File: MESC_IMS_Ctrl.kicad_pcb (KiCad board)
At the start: 2 copper layers, 100 x 75 mm, 194 parts, among them J1 Conn_01x08_Female, J10 Conn_01x04_Male, J2 Conn_01x08_Female, J3 Conn_01x08_Female, J4 Conn_01x06_Male, J5 Conn_ARM_JTAG_SWD_10, J6 USB_C_Receptacle_USB2.0, J7 Conn_01x03_Male, J8 Conn_01x04_Male, J9 Conn_01x08_Male, U1 STM32F303CBTx, U10 TPS61041DBV, U2 LM5017MR, U3 TPS76333, U4 INA240A1PW, U5 UCC21520DW, U6 INA240A1PW, U7 UCC21520DW, U8 INA240A1PW, U9 UCC21520DW, Y1 ASE-8.000MHZ-LC-T

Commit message: More routing
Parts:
- moved TP4 9.06 mm to (132.2, 85.5)
- moved R40 3.05 mm to (112.5, 114.0), turned to 270 degrees
- moved R27 1.46 mm to (128.2, 134.0), turned to 0 degrees
- moved R41 1.34 mm to (112.5, 116.0), turned to 270 degrees
- moved C15 1.27 mm to (128.2, 135.2)
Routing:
- net /ISU_MCU: track 14.7 -> 60.9 mm, vias 0 -> 2
- net /U_I_SEN: track 13.1 -> 57.4 mm, vias 0 -> 2
- net /W_V_SEN: track 96.0 -> 122.5 mm, vias 1 -> 2
- net /V_SEN: track 101.3 -> 127.6 mm, vias 0 -> 2
- net VDD: track 97.3 -> 122.0 mm, vias 8 -> 10
- net /V_V_SEN: track 74.2 -> 98.4 mm, vias 2 -> 4
- net /PWM_IN: track 48.1 -> 51.0 mm
- net /U_IN_LO: track 40.9 -> 42.0 mm, vias 1 -> 2
- net /U_V_SEN: track 92.0 -> 93.1 mm
- net /U_IN_HI: track 41.7 -> 42.8 mm, vias 1 -> 2
- net +3V3: track 334.0 -> 333.1 mm, vias 30 -> 33
- net /ISV_MCU: track 47.4 -> 46.7 mm
- net /ANA_IN: track 43.7 -> 43.2 mm
- net /TMP_INT: track 67.9 -> 68.3 mm, vias 2 -> 4
- net GND: vias 90 -> 91

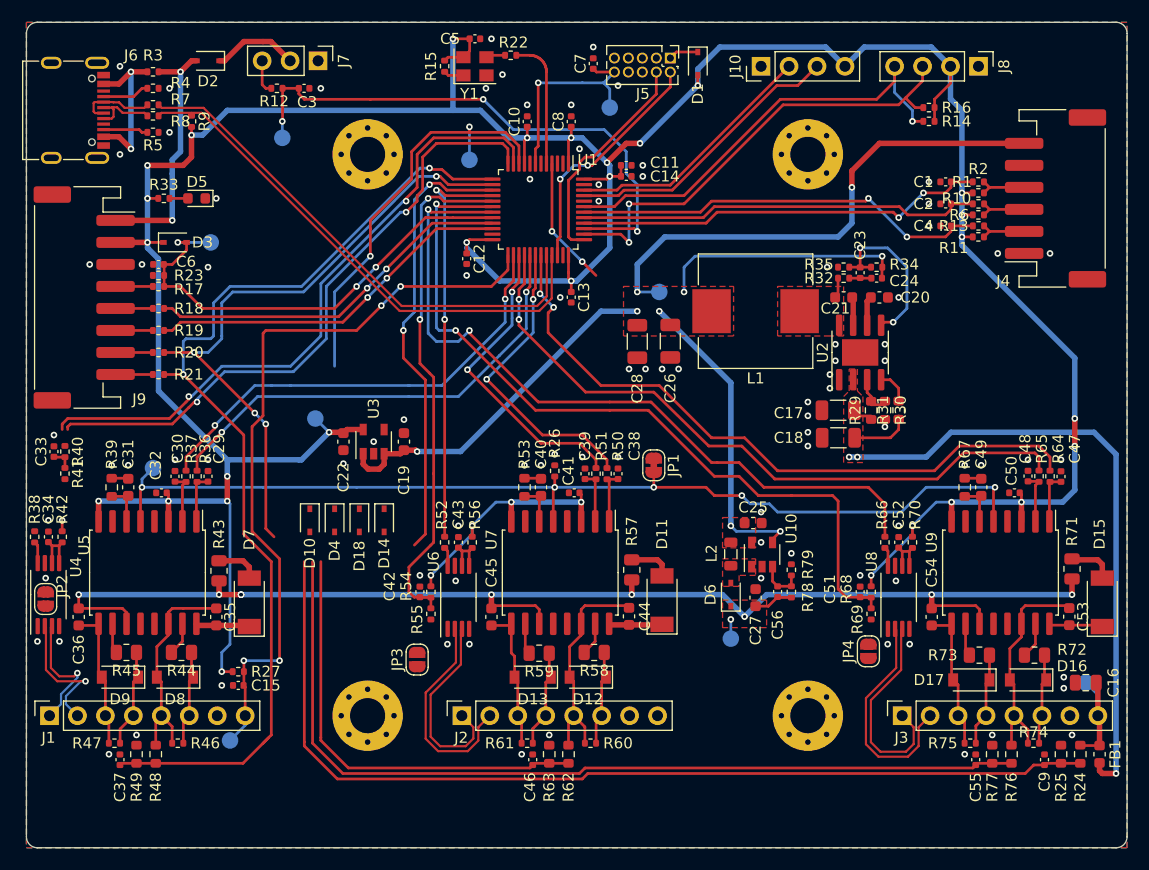
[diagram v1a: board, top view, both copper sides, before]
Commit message: Routing nearly complete
some diodes made smaller
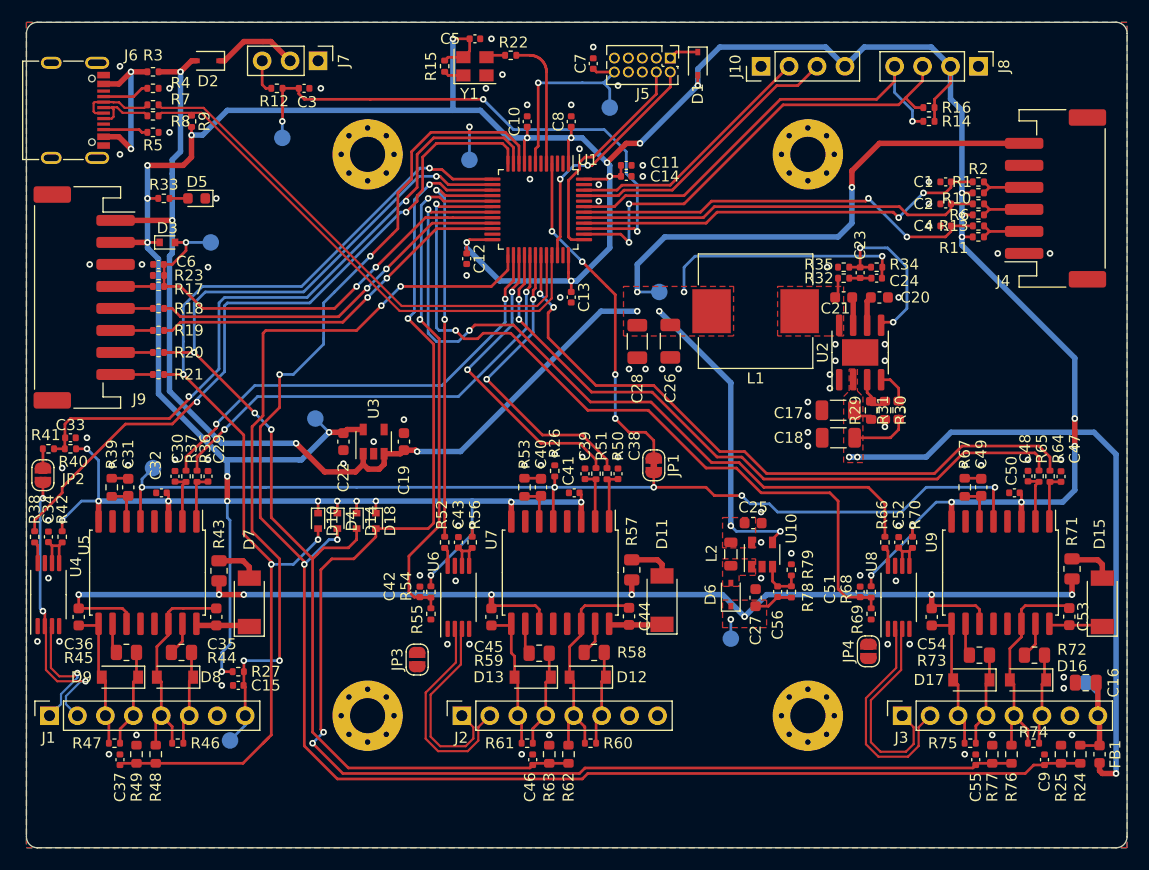
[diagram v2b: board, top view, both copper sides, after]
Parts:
- D10, D14, D18, D3, D4: value NSR1020MW2T1G -> BAT41KFILM; footprint Diode_SMD:D_SOD-323 -> Diode_SMD:D_SOD-523
- moved JP2 11.3 mm to (110.5, 116.2)
- moved R41 2.70 mm to (111.0, 113.8), turned to 180 degrees
- moved D14 2.50 mm to (139.0, 120.3)
- moved C33 1.95 mm to (113.0, 112.8), turned to 0 degrees
- moved D18 1.50 mm to (140.8, 120.3)
- moved D10 0.75 mm to (135.5, 120.3)
- moved D3 0.70 mm to (121.8, 95.0)
- moved R40 0.56 mm to (113.0, 113.8), turned to 180 degrees
- moved D4 0.25 mm to (137.2, 120.3)
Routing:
- net +3V3: track 333.1 -> 371.1 mm, vias 33 -> 38
- net +5V: track 153.5 -> 190.1 mm, vias 11 -> 12
- net /V_SEN: track 127.6 -> 155.4 mm, vias 2 -> 5
- net /GATE_DIS: track 11.8 -> 31.5 mm, vias 2 -> 4
- net /Phase_U/CURR_SEN+: track 12.6 -> 25.9 mm, vias 1 -> 3
- net /V_V_SEN: track 98.4 -> 108.9 mm
- net /W_V_SEN: track 122.5 -> 132.3 mm, vias 2 -> 4
- net /U_I_SEN: track 57.4 -> 65.7 mm
- net /U_V_SEN: track 93.1 -> 99.5 mm, vias 2 -> 4
- net Net-(JP2-Pad2): track 0.00 -> 1.75 mm
- net /W_IN_HI: track 61.2 -> 62.6 mm
- net /ISU_MCU: track 60.9 -> 62.2 mm
- net /ANA_IN: track 43.2 -> 42.6 mm
- net VDD: vias 10 -> 9
- net GND: vias 91 -> 92

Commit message: Adding via stitching and teardrops
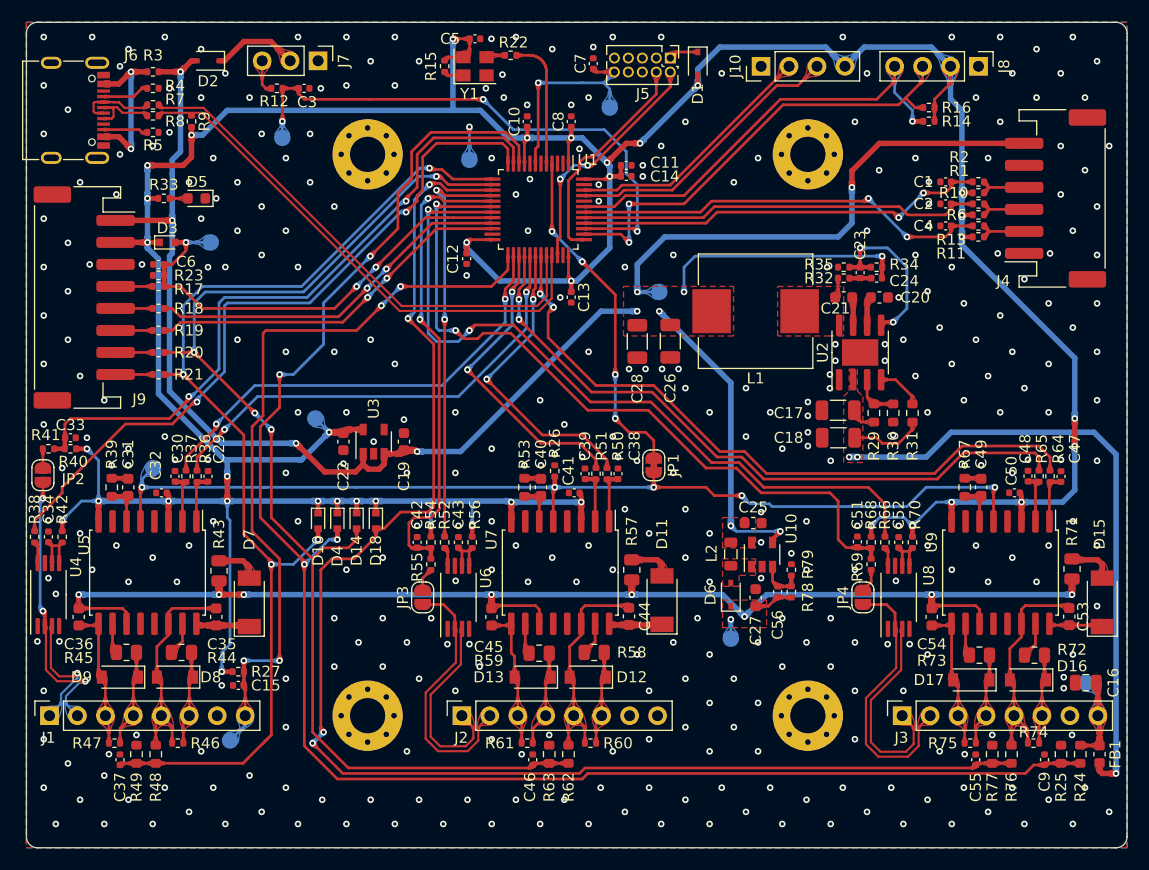
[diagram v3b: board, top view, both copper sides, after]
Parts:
- moved JP3 5.67 mm to (145.0, 127.2)
- moved JP4 4.93 mm to (185.0, 127.2)
- moved C51 4.56 mm to (184.5, 122.2)
- moved C42 4.51 mm to (144.5, 122.2)
- moved R54 4.50 mm to (145.8, 122.2)
- moved R55 4.50 mm to (145.8, 124.2)
- moved R68 4.50 mm to (185.8, 122.2)
- moved R69 4.50 mm to (185.8, 124.2)
- moved R31 1.28 mm to (189.5, 110.5)
- moved R30 0.79 mm to (187.8, 110.5)
- moved R29 0.35 mm to (186.0, 110.5)
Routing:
- net +3V3: track 371.1 -> 365.7 mm
- net /Phase_W/CURR_SEN+: track 20.5 -> 25.2 mm
- net /Phase_V/CURR_SEN+: track 19.5 -> 24.0 mm
- net /ISW_MCU: track 72.2 -> 67.7 mm
- net /ISV_MCU: track 47.2 -> 43.7 mm
- net Net-(JP4-Pad2): track 0.00 -> 2.15 mm
- net Net-(JP3-Pad2): track 0.00 -> 2.15 mm
- net /PSUs/VCC: track 64.6 -> 66.5 mm
- net /W_V_SEN: track 132.3 -> 131.4 mm
- net Net-(R31-Pad2): track 3.40 -> 4.15 mm
- net Net-(R29-Pad2): track 3.68 -> 4.20 mm
- net GND: vias 92 -> 369

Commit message: Updated part numbers
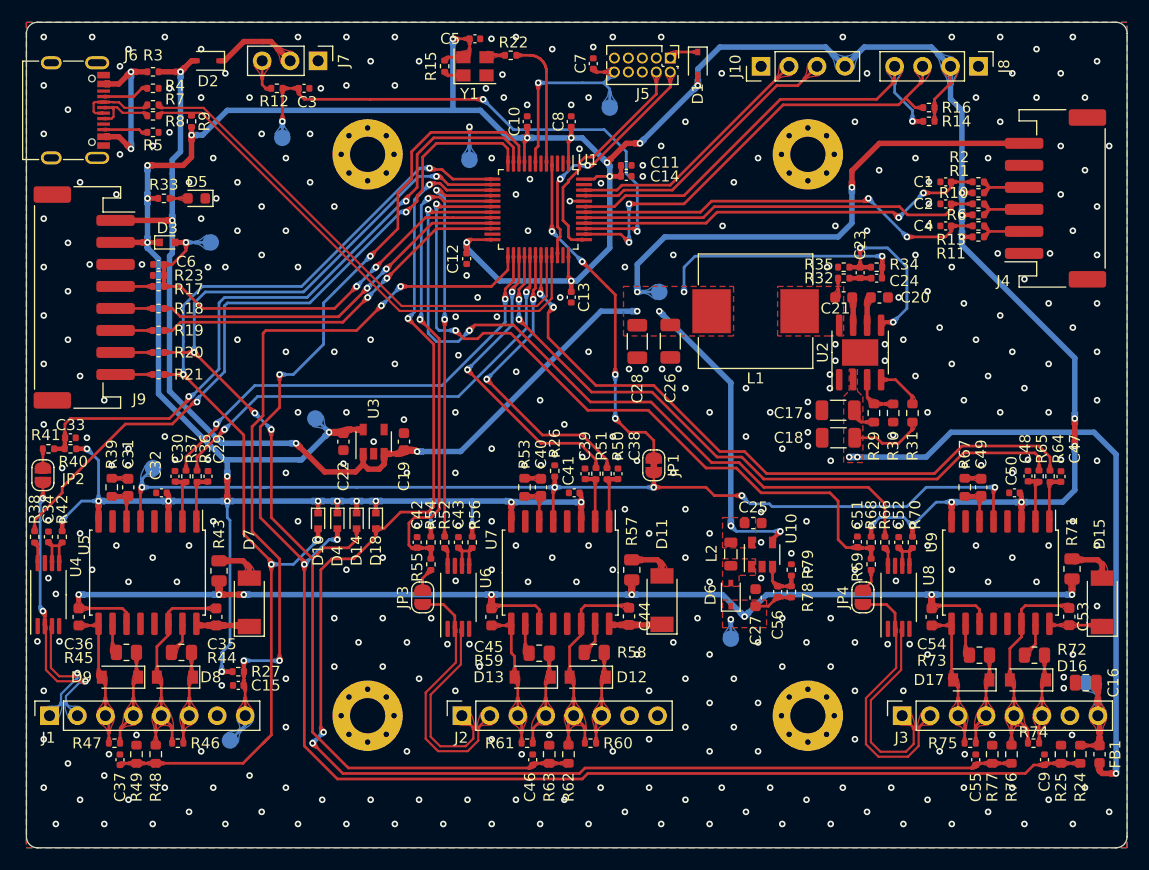
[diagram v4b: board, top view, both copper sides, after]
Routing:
- net GND: track 4.56 -> 5.85 mm, vias 369 -> 376
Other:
- rule via_min_size: 0.3 -> 0.2

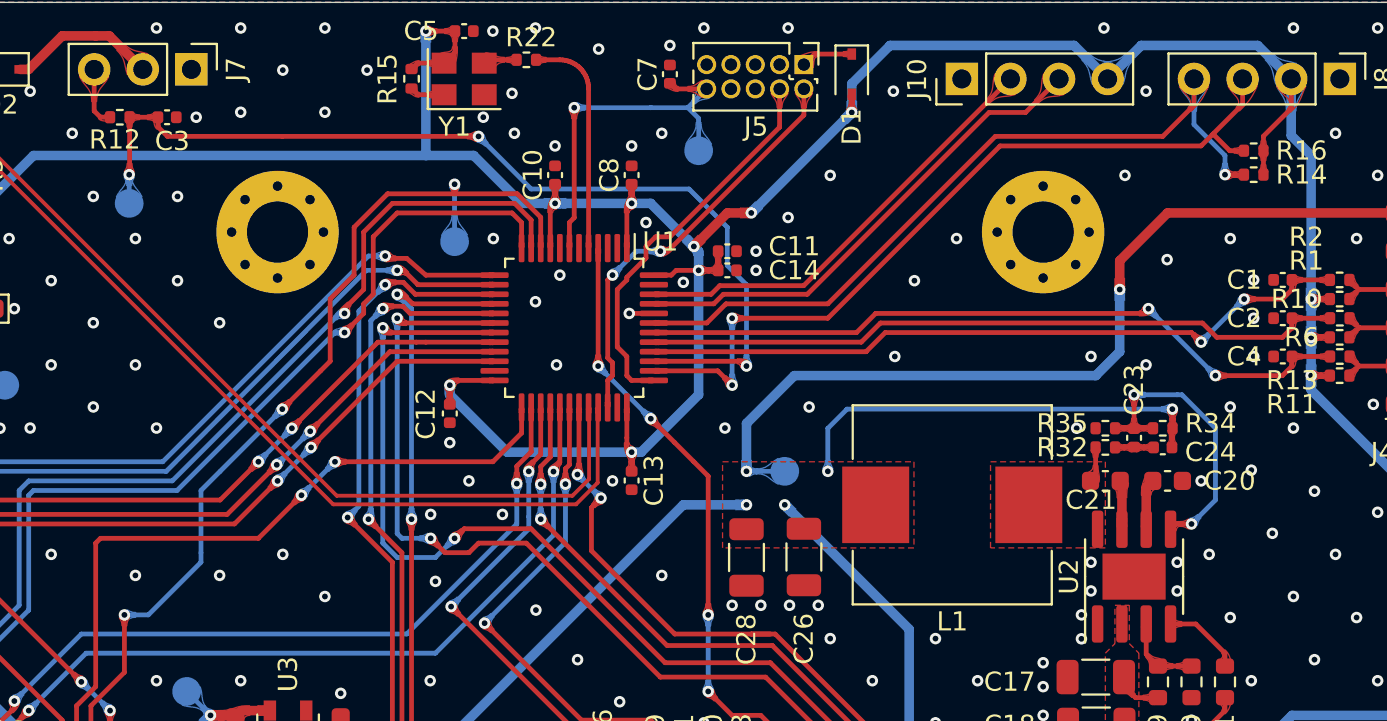
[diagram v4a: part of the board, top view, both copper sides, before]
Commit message: Adding 0V TP and labels
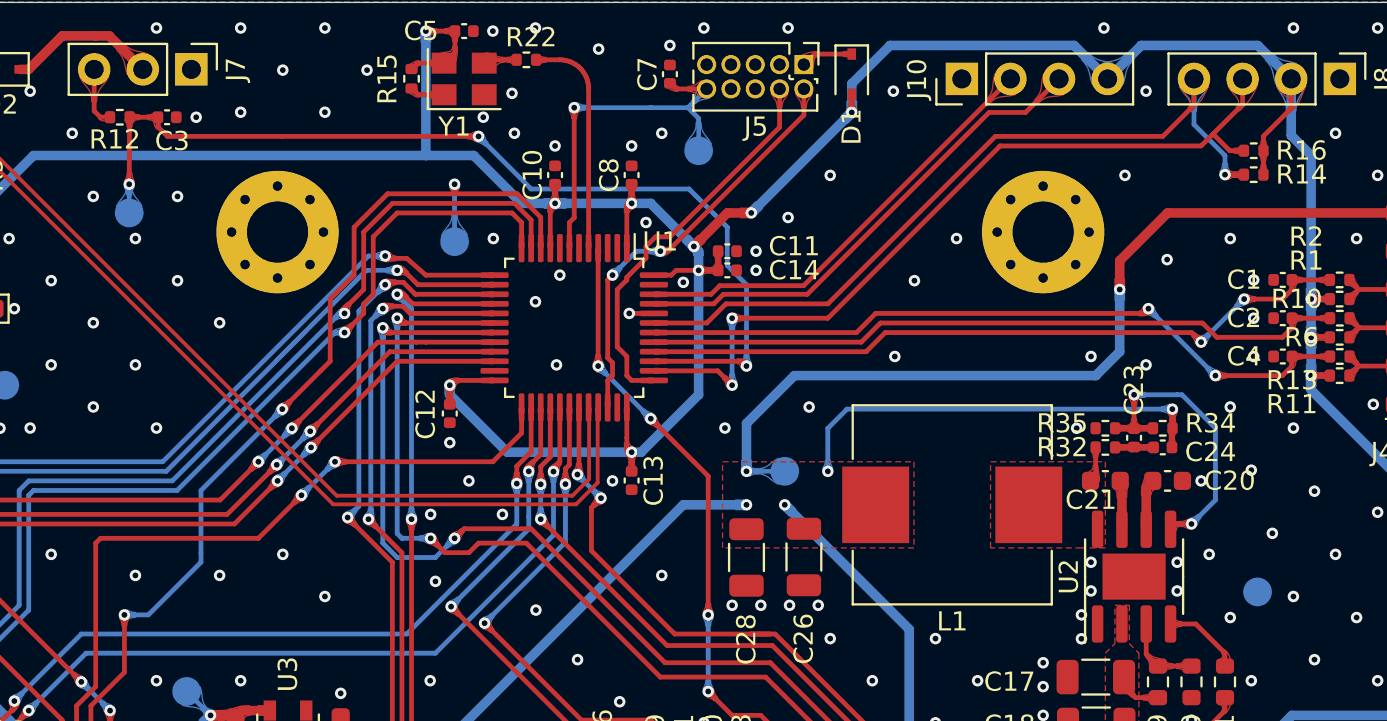
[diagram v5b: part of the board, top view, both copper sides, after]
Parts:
- added TP11: TestPoint, TestPoint:TestPoint_Pad_D1.5mm, B.Cu at (191.2, 105.8)
- added svg2mod: G***, label, B.Cu at (191.2, 103.4)
- added svg2mod: G***, label, B.Cu at (204.2, 96.0)
- added svg2mod: G***, label, B.Cu at (205.2, 131.0)
- added svg2mod: G***, label, B.Cu at (135.2, 108.5)
- added svg2mod: G***, label, B.Cu at (173.0, 128.2)
- added svg2mod: G***, label, B.Cu at (130.4, 82.2)
- added svg2mod: G***, label, B.Cu at (135.5, 82.2)
- added svg2mod: G***, label, B.Cu at (175.8, 83.2)
- added svg2mod: G***, label, B.Cu at (183.4, 83.2)
- added svg2mod: G***, label, B.Cu at (195.5, 83.2)
- added svg2mod: G***, label, B.Cu at (193.0, 83.2)
- added svg2mod: G***, label, B.Cu at (112.6, 101.0)
- added svg2mod: G***, label, B.Cu at (187.9, 83.5)
- added svg2mod: G***, label, B.Cu at (190.4, 83.5)
- added svg2mod: G***, label, B.Cu at (112.6, 103.0)
- added svg2mod: G***, label, B.Cu at (112.6, 99.0)
- added svg2mod: G***, label, B.Cu at (112.5, 95.0)
- added svg2mod: G***, label, B.Cu at (112.6, 97.0)
- added svg2mod: G***, label, B.Cu at (204.2, 94.0)
- added svg2mod: G***, label, B.Cu at (204.2, 92.0)
- added svg2mod: G***, label, B.Cu at (204.2, 90.0)
- added svgemod: G***, label, B.Cu at (112.6, 93.0)
- added svgemod: G***, label, B.Cu at (204.2, 86.0)
- added svgemod: G***, label, B.Cu at (166.5, 97.0)
- added svgemod: G***, label, B.Cu at (133.0, 82.2)
- C10, C11, C12, C13, C23, C32, C34, C41, C43, C5, C50, C52, C6, C7, C8, C9: value 100nF -> 100nF 16V
- C14, C15: value 1uF -> 1uF 25V
- C19, C20: value 1uF 16V -> 1uF 50V
- C31, C40, C49: value C -> 2.2nF
- D11, D15, D7: value D_Schottky_Small -> PMEG10030ELP
- D6: value D -> BAT48JFILM
- R39, R53, R67: value R -> 20k
- R43, R44, R45, R57, R58, R59, R71, R72, R73: value R -> 4R7
- moved TP4 0.50 mm to (132.2, 86.0)
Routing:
- net /PWM_IN: track 51.0 -> 51.5 mm
